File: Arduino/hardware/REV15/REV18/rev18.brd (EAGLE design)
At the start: 50 x 50 mm, 10 parts, among them U1 TC1185SMD

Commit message: up to rev18 roughly
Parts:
- removed +, -: (no value), wirepad:2,15/1,0
- removed C1, C2: 10uF 10V, SparkFun-Passives:0603-CAP
- removed JP1: (no value), jumper:JP1
- removed U1: TC1185SMD, 3.3VREG:TC1185
- removed USBPOWER: MICRO-USB-FCI-10103592, micro-usb-fci-10103592:MICRO-USB-FCI-10103592
- added TMP112: TMP1, TMP112_2:TMP112
- added U$4: SHT21, SHT21:SHT21
- moved U$2 27.9 mm to (-9.03, 25.8)
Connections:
- removed net 5V: C1.1, U1.1, U1.3, USBPOWER.1
- removed net N$8: C2.2, JP1.1, U1.5
- new net SCL: I2C_EXT.9, TMP112.1, U$4.6
- new net SDA: I2C_EXT.11, TMP112.6, U$4.1
- net GND: now also TMP112.2, TMP112.4, U$4.2, U$4.P$1; no longer -.1, C1.2, C2.1, U1.2, USBPOWER.17, USBPOWER.5, USBPOWER.7
- net VCC: now also TMP112.5, U$4.5; no longer +.1, JP1.2
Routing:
- net SCL: track 0.00 -> 51.0 mm
- net SDA: track 0.00 -> 32.8 mm
- net N$8: track 25.2 -> 0.00 mm
- net 5V: track 16.7 -> 0.00 mm, vias 1 -> 0
- net VCC: track 68.2 -> 58.6 mm
- net GND: track 0.00 -> 8.91 mm, vias 4 -> 6
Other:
- board text added: "Pullupresistors are on MCU Board"
- board text added: "SHT21"
- board text removed: "Remove jumper if battery power"

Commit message: up to rev18 cleaned up
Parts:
- added IC1: DS1820, DS1820:TO-92
- moved U$4 25.5 mm to (3.81, 26.7), turned to 270 degrees
- moved TMP112 20.1 mm to (3.81, 35.6), turned to 270 degrees
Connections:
- new net DQ: I2C_EXT.17
- net GND: now also IC1.1
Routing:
- net VCC: track 58.6 -> 48.5 mm, vias 0 -> 2
- net SCL: track 51.0 -> 41.7 mm, vias 0 -> 1
- net SDA: track 32.8 -> 32.4 mm, vias 0 -> 2
- net GND: track 8.91 -> 8.87 mm, vias 6 -> 4
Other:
- board text added: "Pullup resistors are on MCU Board"
- board text removed: "Pullupresistors are on MCU Board"

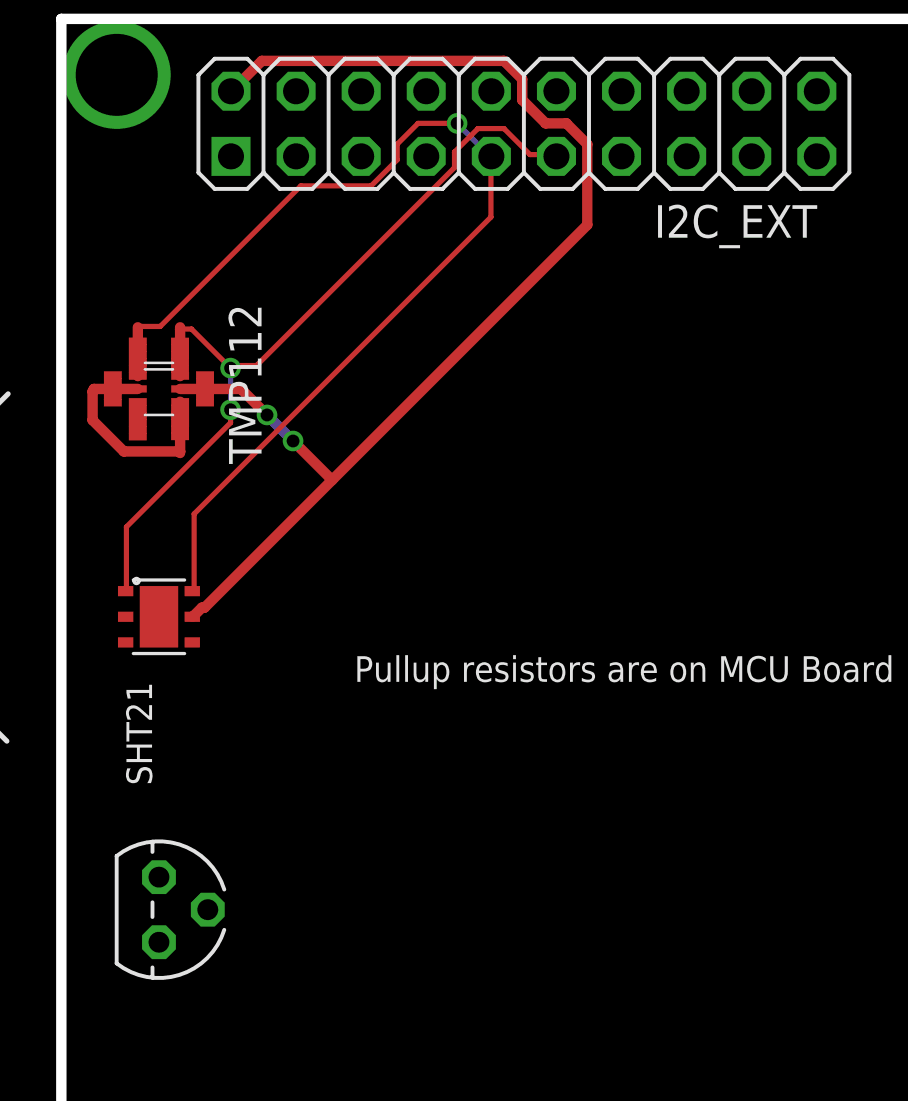
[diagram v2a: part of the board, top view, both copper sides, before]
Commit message: up to rev18 DRC check and ground plane
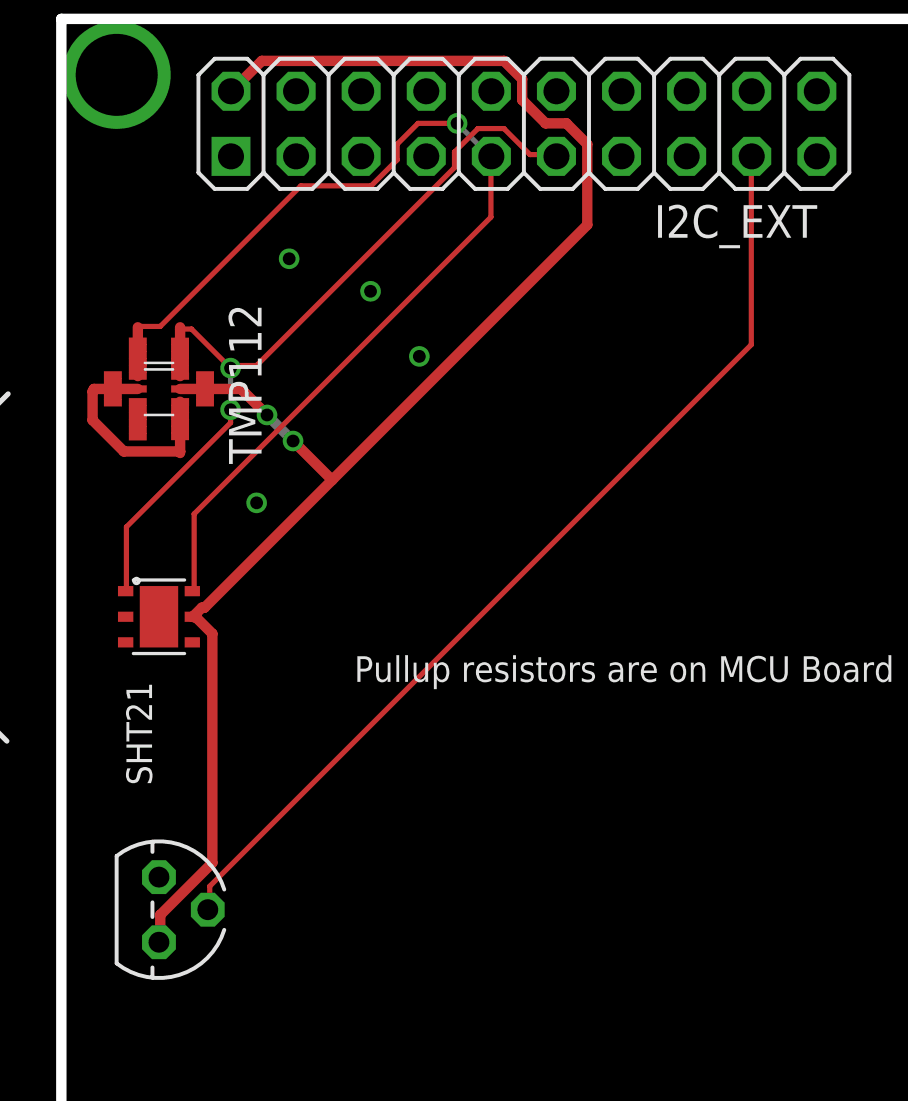
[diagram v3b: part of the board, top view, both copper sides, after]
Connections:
- net DQ: now also IC1.2
- net VCC: now also IC1.3
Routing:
- net DQ: track 0.00 -> 38.2 mm
- net VCC: track 48.5 -> 62.5 mm
- net GND: vias 4 -> 8
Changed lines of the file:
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@@
 <via x="8.0264" y="34.544" extent="1-16" drill="0.5"/>
 <via x="9.0424" y="33.528" extent="1-16" drill="0.5"/>
+<contactref element="IC1" pad="3"/>
+<wire x1="3.8608" y1="15.0368" x2="3.8608" y2="14.0208" width="0.4064" layer="1"/>
+<wire x1="5.8928" y1="17.0688" x2="3.8608" y2="15.0368" width="0.4064" layer="1"/>
+<wire x1="5.8928" y1="26.0096" x2="5.8928" y2="17.0688" width="0.4064" layer="1"/>
+<wire x1="5.2832" y1="26.6192" x2="5.8928" y2="26.0096" width="0.4064" layer="1"/>
+<wire x1="3.8608" y1="14.0208" x2="3.81" y2="13.97" width="0.4064" layer="1"/>
+<wire x1="5.2832" y1="26.6192" x2="5.11" y2="26.67" width="0.4064" layer="1"/>
 </signal>
 <signal name="GND" class="1">
@@
 <wire x1="4.635" y1="33.1216" x2="2.4384" y2="33.1216" width="0.4064" layer="1"/>
 <wire x1="1.2192" y1="35.4584" x2="1.27" y2="35.56" width="0.4064" layer="1"/>
+<via x="8.89" y="40.64" extent="1-16" drill="0.5"/>
+<via x="12.065" y="39.37" extent="1-16" drill="0.5"/>
+<via x="13.97" y="36.83" extent="1-16" drill="0.5"/>
+<via x="7.62" y="31.115" extent="1-16" drill="0.5"/>
 </signal>
 <signal name="32KHZ">
@@
 <signal name="DQ">
 <contactref element="I2C_EXT" pad="17"/>
+<contactref element="IC1" pad="2"/>
+<wire x1="5.7912" y1="16.1544" x2="5.7912" y2="15.24" width="0.2032" layer="1"/>
+<wire x1="26.924" y1="37.2872" x2="5.7912" y2="16.1544" width="0.2032" layer="1"/>
+<wire x1="26.924" y1="44.6024" x2="26.924" y2="37.2872" width="0.2032" layer="1"/>
+<wire x1="5.7912" y1="15.24" x2="5.715" y2="15.24" width="0.2032" layer="1"/>
+<wire x1="26.924" y1="44.6024" x2="26.94" y2="44.635" width="0.2032" layer="1"/>
 </signal>
 </signals>

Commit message: REV15-18 cleaned up, need sanity check
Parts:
- moved U$2 48.7 mm to (39.2, 32.2)
- moved U$1 34.2 mm to (22.3, 7.14)
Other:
- board text added: "20160229"
- board text removed: "20151208"
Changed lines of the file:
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@@
 <board>
 <plain>
-<text x="-5.318971875" y="13.33876875" size="1" layer="25" font="vector" rot="R180">20151208</text>
+<text x="47.62123125" y="13.731028125" size="1" layer="25" font="vector" rot="R270">20160229</text>
 <text x="36.849196875" y="2.125621875" size="1" layer="22" font="vector" rot="MR0">License: http://goo.gl/3d71UJ</text>
 <text x="28.843878125" y="3.10453125" size="1" layer="25" font="vector" rot="R180">OpenTRV.org.uk</text>
@@
 </autorouter>
 <elements>
-<element name="U$2" library="logo" package="TONNE" value="" x="-9.025" y="25.81711875"/>
-<element name="U$1" library="ohw-logo" package="OSHW_10X200_NOTEXT" value="" x="-10.725834375" y="16.02610625"/>
+<element name="U$2" library="logo" package="TONNE" value="" x="39.235" y="32.16711875"/>
+<element name="U$1" library="ohw-logo" package="OSHW_10X200_NOTEXT" value="" x="22.294165625" y="7.13610625"/>
 <element name="I2C_EXT" library="pinhead" package="2X10" value="" x="18.05" y="45.905" smashed="yes">
 <attribute name="NAME" x="23.13" y="41.46" size="1.27" layer="25" ratio="10"/>
